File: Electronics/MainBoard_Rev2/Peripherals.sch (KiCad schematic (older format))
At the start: 17 parts, among them J4 Conn_01x04_Male, Q30 PMBT2222A, Q35 PMBT2222A, U3 LSM6DS3

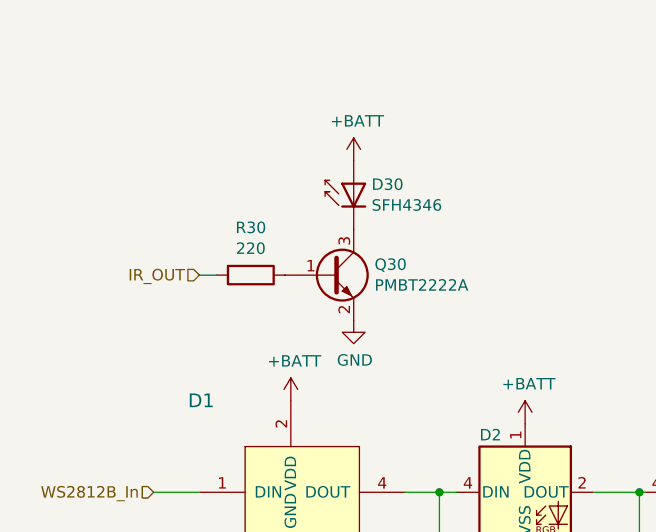
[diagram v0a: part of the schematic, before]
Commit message: Last changes for a functional Lasertag, ordered!
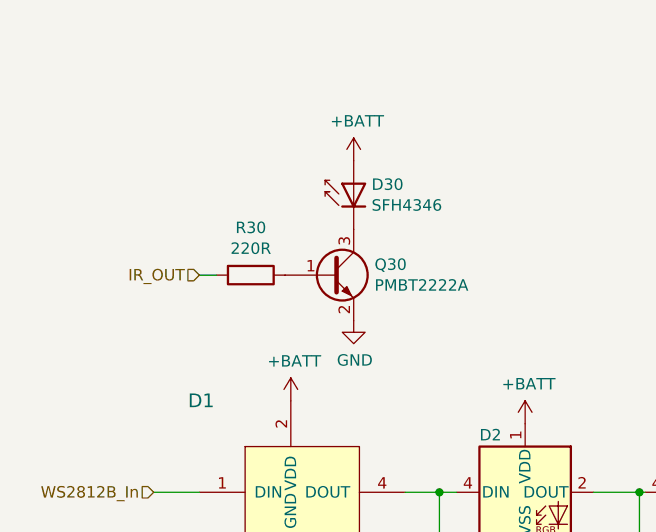
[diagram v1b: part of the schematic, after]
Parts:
- D2: Digi-Key 1528-1104-ND -> (none); Digi-Key_PN (none) -> 1528-1104-ND
- D30: Digi-Key 475-3581-ND -> (none); Digi-Key_PN (none) -> 475-3581-ND
- D35: Digi-Key_PN (none) -> CD0603-B0340RCT-ND
- J4: Digi-Key_PN (none) -> 1568-1827-ND
- Q30, Q35: Digi-Key_PN (none) -> 1727-2956-1-ND; DigiKey 1727-2956-1-ND -> (none)
- R30: value 220 -> 220R
- TRGR1: Digi-Key_PN (none) -> EG1701-ND
- U3: Digi-Key_PN (none) -> 497-15383-1-ND
- VBR1: Digi-Key 1597-1244-ND -> (none); Digi-Key_PN (none) -> 1597-1244-ND
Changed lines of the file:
@@
 F 2 "LED_SMD:LED_WS2812B_PLCC4_5.0x5.0mm_P3.2mm" H 3550 3200 50  0001 L TNN
 F 3 "https://cdn-shop.adafruit.com/datasheets/WS2812B.pdf" H 3600 3125 50  0001 L TNN
-F 4 "1528-1104-ND" H 3500 3500 50  0001 C CNN "Digi-Key"
+F 4 "1528-1104-ND" H 3500 3500 50  0001 C CNN "Digi-Key_PN"
 	1    3500 3500
 	1    0    0    -1
@@
 F 2 "Connector_PinHeader_2.54mm:PinHeader_1x02_P2.54mm_Vertical" H 9675 5050 50  0001 C CNN
 F 3 "" H 9675 5050 50  0001 C CNN
+F 4 "EG1701-ND" H 9675 4850 50  0001 C CNN "Digi-Key_PN"
 	1    9675 4850
 	1    0    0    -1
@@
 F 2 "Package_TO_SOT_SMD:SOT-23" H 8300 5275 50  0001 L CIN
 F 3 "http://www.onsemi.com/pub_link/Collateral/2N3055-D.PDF" H 8100 5350 50  0001 L CNN
-F 4 "1727-2956-1-ND" H 8100 5350 50  0001 C CNN "DigiKey"
+F 4 "1727-2956-1-ND" H 8100 5350 50  0001 C CNN "Digi-Key_PN"
 	1    8100 5350
 	1    0    0    -1
@@
 F 3 "~" H 8550 4710 50  0001 C CNN
 F 4 "316040001" V 8550 4800 50  0001 C CNN "MPN"
-F 5 "1597-1244-ND" V 8550 4800 50  0001 C CNN "Digi-Key"
+F 5 "1597-1244-ND" V 8550 4800 50  0001 C CNN "Digi-Key_PN"
 	1    8550 4800
 	0    1    1    0
@@
 F 2 "Diode_SMD:D_0603_1608Metric" H 8500 5025 50  0001 C CNN
 F 3 "~" H 8500 5025 50  0001 C CNN
+F 4 "CD0603-B0340RCT-ND" H 8500 5025 50  0001 C CNN "Digi-Key_PN"
 	1    8500 5025
 	-1   0    0    1
@@
 F 2 "Package_TO_SOT_SMD:SOT-23" H 2850 2475 50  0001 L CIN
 F 3 "http://www.onsemi.com/pub_link/Collateral/2N3055-D.PDF" H 2650 2550 50  0001 L CNN
-F 4 "1727-2956-1-ND" H 2650 2550 50  0001 C CNN "DigiKey"
+F 4 "1727-2956-1-ND" H 2650 2550 50  0001 C CNN "Digi-Key_PN"
 	1    2650 2550
 	1    0    0    -1
@@
 F 2 "LED_THT:LED_D3.0mm_IRBlack" H 2750 2325 50  0001 C CNN
 F 3 "http://cdn-reichelt.de/documents/datenblatt/A500/SFH4346.pdf" H 2700 2150 50  0001 C CNN
-F 4 "475-3581-ND" V 2750 2150 50  0001 C CNN "Digi-Key"
+F 4 "475-3581-ND" V 2750 2150 50  0001 C CNN "Digi-Key_PN"
 F 5 "SFH 4346" V 2750 2150 50  0001 C CNN "MPN"
 	1    2750 2150
@@
 P 2300 2550
 F 0 "R30" V 2093 2550 50  0000 C CNN
-F 1 "220" V 2184 2550 50  0000 C CNN
+F 1 "220R" V 2184 2550 50  0000 C CNN
 F 2 "Resistor_SMD:R_0805_2012Metric" V 2230 2550 50  0001 C CNN
 F 3 "~" H 2300 2550 50  0001 C CNN
@@
 F 2 "Package_LGA:LGA-14_3x2.5mm_P0.5mm_LayoutBorder3x4y" H 6400 1550 50  0001 L CNN
 F 3 "www.st.com/resource/en/datasheet/lsm6ds3.pdf" H 6900 1600 50  0001 C CNN
+F 4 "497-15383-1-ND" H 6800 2250 50  0001 C CNN "Digi-Key_PN"
 	1    6800 2250
 	1    0    0    -1
@@
 F 2 "MainBoard_Rev2:nav_switch_COM_08184" H 3800 6325 50  0001 C CNN
 F 3 "~" H 3800 6325 50  0001 C CNN
+F 4 "1568-1827-ND" H 3800 6325 50  0001 C CNN "Digi-Key_PN"
 	1    3800 6325
 	1    0    0    -1

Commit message: Modify board for the v3.3 release-ish
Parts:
- removed D35: D_Schottky, Diode_SMD:D_0603_1608Metric, symbol Device:D_Schottky
- removed Q35: PMBT2222A, Package_TO_SOT_SMD:SOT-23, symbol Transistor_BJT:2N3055
- removed R35: 2.2k, Resistor_SMD:R_0805_2012Metric, symbol Device:R_Small
- added C401: 1uF, Capacitor_SMD:C_0805_2012Metric, symbol Device:C_Small
- added D401, D402: IN-PI42TAS, XasPrints:IN-PI42TAS, symbol LED:WS2812B
- added U401: DRV2605, Package_SO:VSSOP-10_3x3mm_P0.5mm, symbol XasParts:DRV2605
- D1: footprint digikey-footprints:LED_RGB_WP154A4SUREQBFZGC -> Connector_PinHeader_2.00mm:PinHeader_1x04_P2.00mm_Vertical
- D30: value SFH4346 -> SFH4545; footprint LED_THT:LED_D3.0mm_IRBlack -> Connector_PinHeader_2.00mm:PinHeader_1x02_P2.00mm_Vertical
- U3: value LSM6DS3 -> LSM6DSMTR
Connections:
- net +BATT: now also D401.1 (VDD), D402.1 (VDD), U401.10 (VDD), U401.5 (EN); no longer VBR1.1 (+)
- net GND: now also C401.2, D401.3 (VSS), D402.3 (VSS), U401.4 (IN), U401.8 (GND)
- net SCL: now also U401.2 (SCL)
- net SDA: now also U401.3 (SDA)
- net WS2812B_Out: now also D402.2 (DOUT); no longer D4.2 (DOUT)
- net at VBR1.2 (-): now also U401.9 (OUT-)
- net at D5.2 (DOUT): now also D401.4 (DIN)
- new net: U401.7 (OUT+), VBR1.1 (+)
- new net: D401.2 (DOUT), D402.4 (DIN)
- new net: C401.1, U401.1 (REG)
- no-connect marks 4 -> 5
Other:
- moved on the sheet: D1, D2, D3, D4, D5, VBR1
